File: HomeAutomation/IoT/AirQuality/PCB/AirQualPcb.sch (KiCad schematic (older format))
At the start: 2 parts

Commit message: AirQual enclosure has parts positioned, PCB is just an initial drawing
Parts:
- removed J?: CONN_04, 1X04, symbol SparkFun-Connectors:CONN_04
- added J1, J2: QWIIC_CONNECTORJS-1MM, Connector_JST:JST_SH_SM04B-SRSS-TB_1x04-1MP_P1.00mm_Horizontal, symbol SparkFun-Connectors:QWIIC_CONNECTORJS-1MM
- added J3: Power Switch, Connectors:1X02, symbol SparkFun-Connectors:CONN_02
- added Q1: ZXMN2B14FHCT, digikey-footprints:SOT-23-3, symbol Device:Q_NMOS_GSD
- added R1: 270K, Resistor_SMD:R_0603_1608Metric, symbol SparkFun-Resistors:RESISTOR0603
- gave numbers to parts that had none: 1
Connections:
- wire segments 11 -> 35
- no-connect marks 0 -> 22
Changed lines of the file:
@@
 $Descr A4 11693 8268
 encoding utf-8
-Sheet 1 1
+Sheet 1 2
 Title ""
 Date ""
@@
 $EndDescr
 $Comp
-L JohnZPCB:Particle_Argon REF?
+L power:GND #PWR0101
+U 1 1 5FDEA0C9
+P 5950 3050
+F 0 "#PWR0101" H 5950 2800 50  0001 C CNN
+F 1 "GND" V 5955 2922 50  0000 R CNN
+F 2 "" H 5950 3050 50  0001 C CNN
+F 3 "" H 5950 3050 50  0001 C CNN
+	1    5950 3050
+	0    1    1    0
+$EndComp
+Text GLabel 6000 2850 0    50   Input ~ 0
+3V3
+Wire Wire Line
+	6200 2850 6000 2850
+$Comp
+L JohnZPCB:Particle_Argon U1
 U 1 1 5FDE89DE
 P 6650 3500
-F 0 "REF?" H 6650 4865 50  0000 C CNN
-F 1 "Particle_Argon" H 6650 4774 50  0000 C CNN
+F 0 "U1" H 6650 4400 50  0000 C CNN
+F 1 "Particle_Argon" H 6650 2650 50  0000 C CNN
 F 2 "JohnZPCB:ParticleArgon" H 6700 3000 50  0001 C CNN
 F 3 "https://docs.particle.io/datasheets/wi-fi/argon-datasheet/" H 6650 4750 50  0001 C CNN
@@
 $EndComp
 Wire Wire Line
-	6200 2700 5850 2900
-$Comp
-L power:GND #PWR0101
-U 1 1 5FDEA0C9
-P 5850 2900
-F 0 "#PWR0101" H 5850 2650 50  0001 C CNN
-F 1 "GND" V 5855 2772 50  0000 R CNN
-F 2 "" H 5850 2900 50  0001 C CNN
-F 3 "" H 5850 2900 50  0001 C CNN
-	1    5850 2900
+	7950 4150 8050 4150
+Wire Wire Line
+	7950 4650 7950 4150
+Wire Wire Line
+	7800 4050 8000 4050
+Wire Wire Line
+	7850 4350 8050 4350
+Wire Wire Line
+	7850 4850 7850 4350
+Wire Wire Line
+	8050 4850 7850 4850
+Wire Wire Line
+	7900 4250 7100 4250
+Wire Wire Line
+	7900 4750 7900 4250
+Wire Wire Line
+	8050 4750 7900 4750
+Wire Wire Line
+	8050 4650 7950 4650
+Wire Wire Line
+	8000 4550 8000 4050
+Wire Wire Line
+	8050 4550 8000 4550
+$Comp
+L SparkFun-Connectors:QWIIC_CONNECTORJS-1MM J2
+U 1 1 5FE3A114
+P 8150 4550
+F 0 "J2" H 7922 4605 45  0000 R CNN
+F 1 "QWIIC_CONNECTORJS-1MM" H 7922 4689 45  0000 R CNN
+F 2 "Connector_JST:JST_SH_SM04B-SRSS-TB_1x04-1MP_P1.00mm_Horizontal" H 8150 5050 20  0001 C CNN
+F 3 "" H 8150 4550 50  0001 C CNN
+F 4 "CONN-13694" H 7922 4784 60  0000 R CNN "Field4"
+	1    8150 4550
+	-1   0    0    1
+$EndComp
+$Comp
+L power:GND #PWR0102
+U 1 1 5FE322C2
+P 7800 4050
+F 0 "#PWR0102" H 7800 3800 50  0001 C CNN
+F 1 "GND" V 7805 3922 50  0000 R CNN
+F 2 "" H 7800 4050 50  0001 C CNN
+F 3 "" H 7800 4050 50  0001 C CNN
+	1    7800 4050
 	0    1    1    0
 $EndComp
-$Comp
-L SparkFun-Connectors:CONN_04 J?
-U 1 1 5FDF72DD
-P 8100 4250
-F 0 "J?" H 7872 4495 45  0000 R CNN
-F 1 "CONN_04" H 7872 4411 45  0000 R CNN
-F 2 "1X04" H 8100 4750 20  0001 C CNN
-F 3 "" H 8100 4250 50  0001 C CNN
-F 4 "CONN-09696" H 7872 4316 60  0000 R CNN "Field4"
-	1    8100 4250
+Connection ~ 8000 4050
+Wire Wire Line
+	8050 4050 8000 4050
+Connection ~ 7850 4350
+Wire Wire Line
+	7500 4350 7850 4350
+Wire Wire Line
+	7500 4150 7500 4350
+Wire Wire Line
+	7100 4150 7500 4150
+Connection ~ 7900 4250
+Wire Wire Line
+	8050 4250 7900 4250
+Connection ~ 7950 4150
+Wire Wire Line
+	7800 4150 7950 4150
+Text GLabel 7800 4150 0    50   Input ~ 0
+3V3
+$Comp
+L SparkFun-Connectors:QWIIC_CONNECTORJS-1MM J1
+U 1 1 5FE2FDB0
+P 8150 4050
+F 0 "J1" H 7922 4105 45  0000 R CNN
+F 1 "QWIIC_CONNECTORJS-1MM" H 7922 4189 45  0000 R CNN
+F 2 "Connector_JST:JST_SH_SM04B-SRSS-TB_1x04-1MP_P1.00mm_Horizontal" H 8150 4550 20  0001 C CNN
+F 3 "" H 8150 4050 50  0001 C CNN
+F 4 "CONN-13694" H 7922 4284 60  0000 R CNN "Field4"
+	1    8150 4050
+	-1   0    0    1
+$EndComp
+NoConn ~ 6200 3150
+NoConn ~ 6200 3250
+NoConn ~ 6200 3350
+NoConn ~ 6200 3450
+NoConn ~ 6200 3550
+NoConn ~ 6200 3650
+NoConn ~ 6200 3750
+NoConn ~ 6200 3850
+NoConn ~ 6200 3950
+NoConn ~ 6200 4050
+NoConn ~ 6200 4150
+NoConn ~ 6200 4250
+NoConn ~ 7100 4050
+NoConn ~ 7100 3950
+NoConn ~ 7100 3850
+NoConn ~ 7100 3750
+NoConn ~ 7100 3650
+NoConn ~ 7100 3550
+NoConn ~ 7100 3450
+NoConn ~ 7100 3350
+NoConn ~ 6200 2750
+NoConn ~ 6200 2950
+Wire Wire Line
+	5950 3050 6200 3050
+Wire Wire Line
+	7600 3250 7600 2550
+Wire Wire Line
+	7500 2350 7500 3150
+Wire Wire Line
+	7500 3150 7100 3150
+Wire Wire Line
+	8350 2350 8350 2450
+Wire Wire Line
+	8350 2350 7500 2350
+Wire Wire Line
+	8350 2900 8350 3000
+Connection ~ 8350 2900
+Wire Wire Line
+	8200 2900 8350 2900
+Wire Wire Line
+	7900 3200 7900 3100
+Wire Wire Line
+	7900 2550 7900 2700
+Wire Wire Line
+	8350 2850 8350 2900
+Wire Wire Line
+	7600 2550 7900 2550
+Wire Wire Line
+	8350 3100 8350 3200
+Wire Wire Line
+	8400 3100 8350 3100
+$Comp
+L power:GND #PWR0103
+U 1 1 5FE6E794
+P 8350 3200
+F 0 "#PWR0103" H 8350 2950 50  0001 C CNN
+F 1 "GND" H 8355 3072 50  0000 R CNN
+F 2 "" H 8350 3200 50  0001 C CNN
+F 3 "" H 8350 3200 50  0001 C CNN
+	1    8350 3200
+	1    0    0    -1
+$EndComp
+$Comp
+L power:GND #PWR0104
+U 1 1 5FE6DB96
+P 7900 3200
+F 0 "#PWR0104" H 7900 2950 50  0001 C CNN
+F 1 "GND" H 7905 3072 50  0000 R CNN
+F 2 "" H 7900 3200 50  0001 C CNN
+F 3 "" H 7900 3200 50  0001 C CNN
+	1    7900 3200
+	1    0    0    -1
+$EndComp
+Wire Wire Line
+	8350 3000 8400 3000
+$Comp
+L Device:Q_NMOS_GSD Q1
+U 1 1 5FE6415E
+P 8000 2900
+F 0 "Q1" H 8206 2900 50  0000 L CNN
+F 1 "ZXMN2B14FHCT" H 8206 2855 50  0001 L CNN
+F 2 "digikey-footprints:SOT-23-3" H 8200 3000 50  0001 C CNN
+F 3 "https://www.diodes.com/assets/Datasheets/ZXMN2B14FH.pdf" H 8000 2900 50  0001 C CNN
+	1    8000 2900
 	-1   0    0    -1
 $EndComp
 $Comp
-L power:GND #PWR?
-U 1 1 5FDF82F0
-P 7950 4350
-F 0 "#PWR?" H 7950 4100 50  0001 C CNN
-F 1 "GND" H 7955 4177 50  0000 C CNN
-F 2 "" H 7950 4350 50  0001 C CNN
-F 3 "" H 7950 4350 50  0001 C CNN
-	1    7950 4350
-	1    0    0    -1
-$EndComp
-Wire Wire Line
-	8000 4250 7950 4250
-Wire Wire Line
-	7950 4250 7950 4350
-Wire Wire Line
-	8000 4150 7350 4150
-Wire Wire Line
-	7350 4150 7350 3900
-Wire Wire Line
-	7350 3900 7100 3900
-Wire Wire Line
-	7100 3800 7450 3800
-Wire Wire Line
-	7450 3800 7450 4050
-Wire Wire Line
-	7450 4050 8000 4050
-Text GLabel 7900 3950 0    50   Input ~ 0
-3V3
-Wire Wire Line
-	7900 3950 8000 3950
-Text GLabel 6000 2500 0    50   Input ~ 0
-3V3
-Wire Wire Line
-	6200 2500 6000 2500
+L SparkFun-Connectors:CONN_02 J3
+U 1 1 5FE5F4F6
+P 8500 3000
+F 0 "J3" H 8272 2955 45  0000 R CNN
+F 1 "Power Switch" H 8272 3039 45  0000 R CNN
+F 2 "Connectors:1X02" H 8500 3250 20  0001 C CNN
+F 3 "" H 8500 3000 50  0001 C CNN
+F 4 "SPST NO" H 8272 3134 60  0000 R CNN "Field4"
+	1    8500 3000
+	-1   0    0    1
+$EndComp
+$Comp
+L SparkFun-Resistors:RESISTOR0603 R1
+U 1 1 5FE5C47B
+P 8350 2650
+F 0 "R1" V 8255 2718 45  0000 L CNN
+F 1 "270K" V 8339 2718 45  0000 L CNN
+F 2 "Resistor_SMD:R_0603_1608Metric" H 8350 2800 20  0001 C CNN
+F 3 "" H 8350 2650 60  0001 C CNN
+F 4 " " V 8434 2718 60  0000 L CNN "Field4"
+	1    8350 2650
+	0    1    1    0
+$EndComp
+Wire Wire Line
+	7100 3250 7600 3250
+$Sheet
+S 7400 5200 1150 850
+U 5FE79CA5
+F0 "SensorsSheet" 50
+F1 "Sensors.sch" 50
+$EndSheet
 $EndSCHEMATC

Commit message: PCB laid-out.  About to start tracks.
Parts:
- removed Q1: ZXMN2B14FHCT, digikey-footprints:SOT-23-3, symbol Device:Q_NMOS_GSD
- added C1, C2, C3, C5: 10uF, Capacitors:0603, symbol Device:C
- added C4, C7, C8, C9: 100nF, Capacitors:0603, symbol Device:C
- added C6: 1uF, Capacitors:0603, symbol Device:C
- added J2: QWIIC_CONNECTORJS-1MM, Connector_JST:JST_SH_SM04B-SRSS-TB_1x04-1MP_P1.00mm_Horizontal, symbol SparkFun-Connectors:QWIIC_CONNECTORJS-1MM
- added J5: UART_CONNECTORJS-1MM, Connectors:1X04_1MM_RA, symbol JohnZPCB:UART_CONNECTORJS-1MM
- added L1: VLS3012HBX-2R2M‎, JohnZPCB:VLS3012HBX, symbol pspice:INDUCTOR
- added Q1, Q2, Q3: BSS138, digikey-footprints:SOT-23-3, symbol dk_Transistors-FETs-MOSFETs-Single:BSS138
- added R2, R3, R4, R5: 10K, 0603, symbol SparkFun-Resistors:RESISTOR0603
- added U1: RP402Nxx1x, Package_TO_SOT_SMD:SOT-23-5, symbol JohnZPCB:RP402Nxx1x
- J1: renamed from J3; footprint Connectors:1X02 -> Connectors:1X03; symbol SparkFun-Connectors:CONN_02 -> SparkFun-Connectors:CONN_03; Field4 SPST NO -> NO/NC
- renumbered J1 to J3, J2 to J4, U1 to U2
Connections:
- net 3V3: now also C5.1, C6.1, C7.1, C8.1, C9.1, J2.2 (VCC), Q2.1 (G), Q3.1 (G), R2.2, R3.2, U1.3 (CE)
- net GND: now also C1.2, C2.2, C3.2, C4.2, C5.2, C6.2, C7.2, C8.2, C9.2, J2.1 (GND), J5.1 (GND), Q1.2 (S), U1.2 (GND)
- net at U2.14 (RX): now also Q2.2 (S), R2.1
- net at U2.15 (TX): now also Q3.2 (S), R3.1
- net at J3.3 (SDA), J4.3 (SDA), U2.17 (SDA): now also J2.3 (SDA)
- net at J3.4 (SCL), J4.4 (SCL), U2.18 (SCK): now also J2.4 (SCL)
- net at U2.27 (EN): now also J1.3, Q1.3 (D)
- net at R1.1, U2.28 (LI+): now also C1.1, L1.1, U1.4 (Vin)
- net at J1.1, R1.2: now also Q1.1 (G)
- new net: L1.2, U1.1 (Lx)
- new net: J5.3 (RX), Q3.3 (D), R5.1
- new net: J5.4 (TX), Q2.3 (D), R4.1
- new net +5V: C2.1, C3.1, C4.1, J5.2 (VCC), R4.2, R5.2, U1.5 (Vout)
- no-connect marks 22 -> 20
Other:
- note added: "Rx & Tx are swapped"
- moved on the sheet: R1

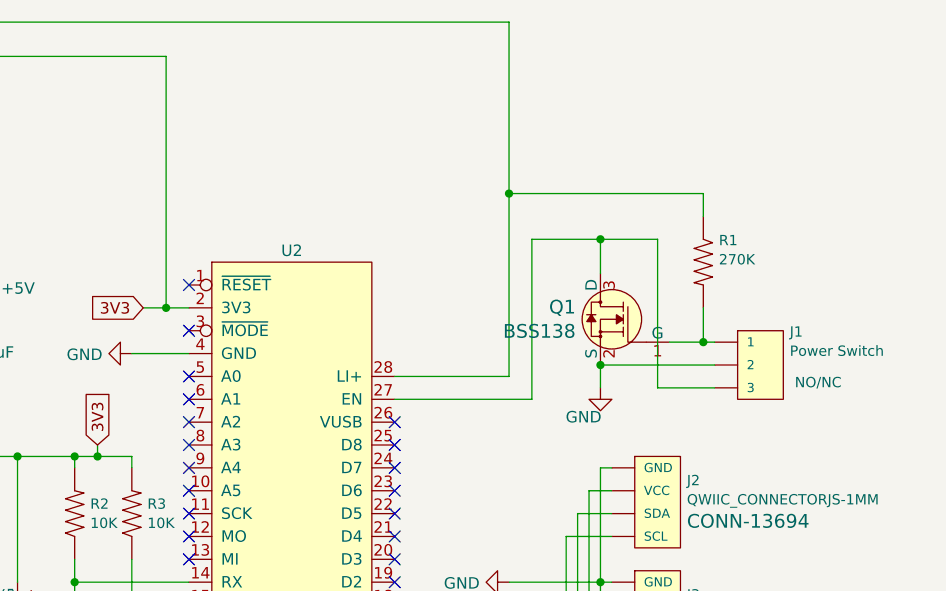
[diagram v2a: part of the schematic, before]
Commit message: Add a fan power connector
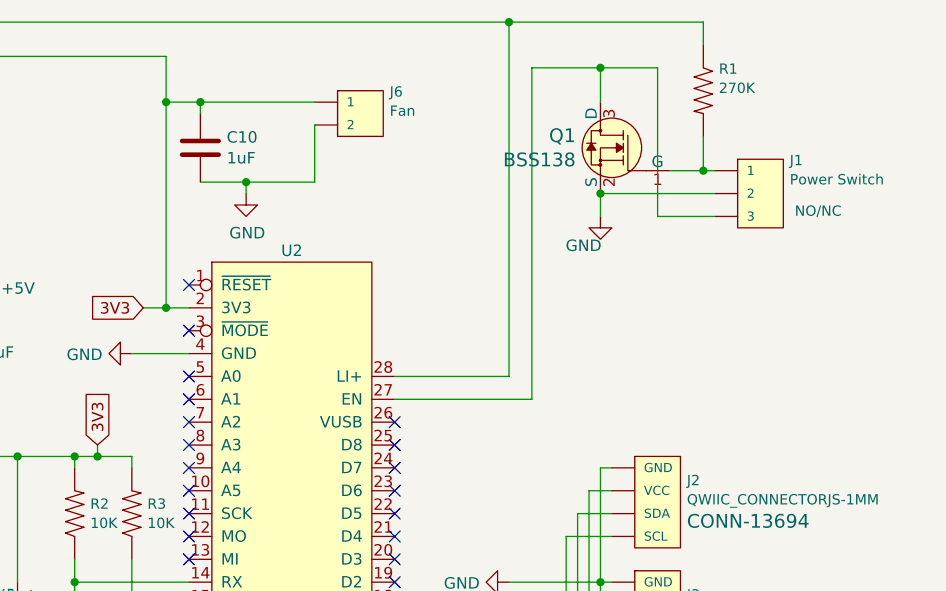
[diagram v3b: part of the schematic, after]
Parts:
- added C10: 1uF, Capacitors:0603, symbol Device:C
- added J6: Fan, Connectors:1X02, symbol SparkFun-Connectors:CONN_02
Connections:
- net 3V3: now also C10.1, J6.1
- net GND: now also C10.2, J6.2
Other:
- moved on the sheet: J1, Q1, R1
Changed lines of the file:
@@
 	5950 3050 6200 3050
 Wire Wire Line
-	7700 3250 7700 2550
-Wire Wire Line
-	7600 2350 7600 3150
-Wire Wire Line
-	8450 2350 8450 2450
-Connection ~ 8450 3000
-Wire Wire Line
-	8450 2850 8450 3000
-Wire Wire Line
-	7700 2550 8000 2550
+	8450 1600 8450 1700
+Connection ~ 8450 2250
+Wire Wire Line
+	8450 2100 8450 2250
+Wire Wire Line
+	7700 1800 8000 1800
 $Comp
 L power:GND #PWR06
 U 1 1 5FE6DB96
-P 8000 3200
-F 0 "#PWR06" H 8000 2950 50  0001 C CNN
-F 1 "GND" H 8005 3072 50  0000 R CNN
-F 2 "" H 8000 3200 50  0001 C CNN
-F 3 "" H 8000 3200 50  0001 C CNN
-	1    8000 3200
-	1    0    0    -1
-$EndComp
-Wire Wire Line
-	8450 3000 8500 3000
+P 8000 2450
+F 0 "#PWR06" H 8000 2200 50  0001 C CNN
+F 1 "GND" H 8005 2322 50  0000 R CNN
+F 2 "" H 8000 2450 50  0001 C CNN
+F 3 "" H 8000 2450 50  0001 C CNN
+	1    8000 2450
+	1    0    0    -1
+$EndComp
+Wire Wire Line
+	8450 2250 8500 2250
 $Comp
 L SparkFun-Resistors:RESISTOR0603 R1
 U 1 1 5FE5C47B
-P 8450 2650
-F 0 "R1" V 8355 2718 45  0000 L CNN
-F 1 "270K" V 8439 2718 45  0000 L CNN
-F 2 "Resistor_SMD:R_0603_1608Metric" H 8450 2800 20  0001 C CNN
-F 3 "" H 8450 2650 60  0001 C CNN
-F 4 " " V 8534 2718 60  0000 L CNN "Field4"
-	1    8450 2650
+P 8450 1900
+F 0 "R1" V 8355 1968 45  0000 L CNN
+F 1 "270K" V 8439 1968 45  0000 L CNN
+F 2 "Resistor_SMD:R_0603_1608Metric" H 8450 2050 20  0001 C CNN
+F 3 "" H 8450 1900 60  0001 C CNN
+F 4 " " V 8534 1968 60  0000 L CNN "Field4"
+	1    8450 1900
 	0    1    1    0
 $EndComp
-Wire Wire Line
-	8500 3200 8250 3200
-Wire Wire Line
-	8250 3200 8250 2550
-Wire Wire Line
-	8250 2550 8000 2550
-Connection ~ 8000 2550
+Connection ~ 8000 1800
 $Comp
 L SparkFun-Connectors:CONN_03 J1
 U 1 1 5FE5F4F6
-P 8600 3000
-F 0 "J1" H 8372 2955 45  0000 R CNN
-F 1 "Power Switch" H 8372 3039 45  0000 R CNN
-F 2 "Connectors:1X03" H 8600 3250 20  0001 C CNN
-F 3 "" H 8600 3000 50  0001 C CNN
-F 4 "NO/NC" H 8350 3150 45  0000 R BNN "Field4"
-	1    8600 3000
+P 8600 2250
+F 0 "J1" H 8372 2205 45  0000 R CNN
+F 1 "Power Switch" H 8372 2289 45  0000 R CNN
+F 2 "Connectors:1X03" H 8600 2500 20  0001 C CNN
+F 3 "" H 8600 2250 50  0001 C CNN
+F 4 "NO/NC" H 8350 2400 45  0000 R BNN "Field4"
+	1    8600 2250
 	-1   0    0    1
 $EndComp
@@
 	4650 2750 4700 2750
 Wire Wire Line
-	8450 2350 7600 2350
+	8450 1600 7600 1600
 $Comp
 L Device:C C9
@@
 	6700 4800 7200 4800
 Wire Wire Line
-	8000 2550 8000 2700
-Connection ~ 8000 3100
-Wire Wire Line
-	8000 3100 8500 3100
-Wire Wire Line
-	8000 3200 8000 3100
-Wire Wire Line
-	8300 3000 8450 3000
+	8000 1800 8000 1950
+Connection ~ 8000 2350
+Wire Wire Line
+	8000 2350 8500 2350
+Wire Wire Line
+	8000 2450 8000 2350
+Wire Wire Line
+	8300 2250 8450 2250
 $Comp
 L dk_Transistors-FETs-MOSFETs-Single:BSS138 Q1
 U 1 1 5FF9946F
-P 8000 2900
-F 0 "Q1" H 8108 2953 60  0000 L CNN
-F 1 "BSS138" H 8108 2847 60  0000 L CNN
-F 2 "digikey-footprints:SOT-23-3" H 8200 3100 60  0001 L CNN
-F 3 "https://www.onsemi.com/pub/Collateral/BSS138-D.PDF" H 8200 3200 60  0001 L CNN
-F 4 "BSS138CT-ND" H 8200 3300 60  0001 L CNN "Digi-Key_PN"
-F 5 "BSS138" H 8200 3400 60  0001 L CNN "MPN"
-F 6 "Discrete Semiconductor Products" H 8200 3500 60  0001 L CNN "Category"
-F 7 "Transistors - FETs, MOSFETs - Single" H 8200 3600 60  0001 L CNN "Family"
-F 8 "https://www.onsemi.com/pub/Collateral/BSS138-D.PDF" H 8200 3700 60  0001 L CNN "DK_Datasheet_Link"
-F 9 "/product-detail/en/on-semiconductor/BSS138/BSS138CT-ND/244294" H 8200 3800 60  0001 L CNN "DK_Detail_Page"
-F 10 "MOSFET N-CH 50V 220MA SOT-23" H 8200 3900 60  0001 L CNN "Description"
-F 11 "ON Semiconductor" H 8200 4000 60  0001 L CNN "Manufacturer"
-F 12 "Active" H 8200 4100 60  0001 L CNN "Status"
-	1    8000 2900
+P 8000 2150
+F 0 "Q1" H 8108 2203 60  0000 L CNN
+F 1 "BSS138" H 8108 2097 60  0000 L CNN
+F 2 "digikey-footprints:SOT-23-3" H 8200 2350 60  0001 L CNN
+F 3 "https://www.onsemi.com/pub/Collateral/BSS138-D.PDF" H 8200 2450 60  0001 L CNN
+F 4 "BSS138CT-ND" H 8200 2550 60  0001 L CNN "Digi-Key_PN"
+F 5 "BSS138" H 8200 2650 60  0001 L CNN "MPN"
+F 6 "Discrete Semiconductor Products" H 8200 2750 60  0001 L CNN "Category"
+F 7 "Transistors - FETs, MOSFETs - Single" H 8200 2850 60  0001 L CNN "Family"
+F 8 "https://www.onsemi.com/pub/Collateral/BSS138-D.PDF" H 8200 2950 60  0001 L CNN "DK_Datasheet_Link"
+F 9 "/product-detail/en/on-semiconductor/BSS138/BSS138CT-ND/244294" H 8200 3050 60  0001 L CNN "DK_Detail_Page"
+F 10 "MOSFET N-CH 50V 220MA SOT-23" H 8200 3150 60  0001 L CNN "Description"
+F 11 "ON Semiconductor" H 8200 3250 60  0001 L CNN "Manufacturer"
+F 12 "Active" H 8200 3350 60  0001 L CNN "Status"
+	1    8000 2150
 	-1   0    0    -1
 $EndComp
@@
 Wire Wire Line
 	3500 1600 7600 1600
-Connection ~ 7600 2350
 $Comp
 L dk_Transistors-FETs-MOSFETs-Single:BSS138 Q2
@@
 Connection ~ 5450 3500
 Wire Wire Line
-	6100 1750 6100 2850
-Wire Wire Line
-	7600 1600 7600 2350
+	6100 1750 6100 1950
 $Comp
 L Device:C C4
@@
 Wire Wire Line
 	7200 4800 7700 4800
+Connection ~ 7600 1600
+Wire Wire Line
+	7600 1600 7600 3150
+Wire Wire Line
+	7700 1800 7700 3250
+Wire Wire Line
+	8250 1800 8000 1800
+Wire Wire Line
+	8500 2450 8250 2450
+Wire Wire Line
+	8250 2450 8250 1800
+$Comp
+L SparkFun-Connectors:CONN_02 J6
+U 1 1 5FF0A496
+P 6850 1950
+F 0 "J6" H 6622 1905 45  0000 R CNN
+F 1 "Fan" H 6622 1989 45  0000 R CNN
+F 2 "Connectors:1X02" H 6850 2200 20  0001 C CNN
+F 3 "" H 6850 1950 50  0001 C CNN
+F 4 "" H 6600 2100 45  0000 R BNN "Field4"
+	1    6850 1950
+	-1   0    0    1
+$EndComp
+Connection ~ 6100 1950
+Wire Wire Line
+	6100 1950 6100 2850
+$Comp
+L Device:C C10
+U 1 1 5FF1CC9B
+P 6250 2150
+F 0 "C10" H 6365 2196 50  0000 L CNN
+F 1 "1uF" H 6365 2105 50  0000 L CNN
+F 2 "Capacitors:0603" H 6288 2000 50  0001 C CNN
+F 3 "https://www.digikey.com/en/products/detail/GRM188R60J106ME47D/490-3896-1-ND/965938?itemSeq=349211413" H 6250 2150 50  0001 C CNN
+	1    6250 2150
+	1    0    0    -1
+$EndComp
+$Comp
+L power:GND #PWR0101
+U 1 1 5FF29F68
+P 6450 2350
+F 0 "#PWR0101" H 6450 2100 50  0001 C CNN
+F 1 "GND" H 6455 2177 50  0000 C CNN
+F 2 "" H 6450 2350 50  0001 C CNN
+F 3 "" H 6450 2350 50  0001 C CNN
+	1    6450 2350
+	1    0    0    -1
+$EndComp
+Wire Wire Line
+	6250 2300 6450 2300
+Wire Wire Line
+	6450 2300 6450 2350
+Wire Wire Line
+	6450 2300 6750 2300
+Wire Wire Line
+	6750 2300 6750 2050
+Connection ~ 6450 2300
+Wire Wire Line
+	6100 1950 6250 1950
+Wire Wire Line
+	6250 2000 6250 1950
+Connection ~ 6250 1950
+Wire Wire Line
+	6250 1950 6750 1950
 $EndSCHEMATC
